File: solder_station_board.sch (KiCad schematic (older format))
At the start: 34 parts, among them J1 Conn_01x04, J2 Conn_FBA, J3 RT_WELLER, J4 VFD dISPLAY, J5 Conn_FBB, P1 ISP, Q1 IRF9540, Q2 2N7002, U4 TLC272, U5 LT1007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

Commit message: Save the last working stand
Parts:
- removed J2: Conn_FBA, Connector_PinSocket_2.54mm:PinSocket_1x01_P2.54mm_Vertical, symbol Connector_Generic:Conn_01x01
- removed J5: Conn_FBB, Connector_PinSocket_2.54mm:PinSocket_1x01_P2.54mm_Vertical, symbol Connector_Generic:Conn_01x01
- added J2: Conn_FB, Connector_PinSocket_2.54mm:PinSocket_1x02_P2.54mm_Vertical, symbol Connector_Generic:Conn_01x02
- added J6: PWR_15V, Connector_Wire:SolderWirePad_1x02_P5.08mm_Drill1.5mm, symbol Connector_Generic:Conn_01x02
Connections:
- wire segments 177 -> 181
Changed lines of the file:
@@
 	9200 5700 8900 5700
 Wire Wire Line
-	9200 6050 8900 6050
-Text Label 9200 6050 2    50   ~ 0
+	9200 5800 8900 5800
+Text Label 9200 5800 2    50   ~ 0
 FBB
-$Comp
-L Connector_Generic:Conn_01x01 J2
-U 1 1 5B5F78C9
-P 8700 5700
-F 0 "J2" H 8620 5475 50  0000 C CNN
-F 1 "Conn_FBA" H 8620 5566 50  0000 C CNN
-F 2 "Connector_PinSocket_2.54mm:PinSocket_1x01_P2.54mm_Vertical" H 8700 5700 50  0001 C CNN
-F 3 "~" H 8700 5700 50  0001 C CNN
-	1    8700 5700
-	-1   0    0    1
-$EndComp
-$Comp
-L Connector_Generic:Conn_01x01 J5
-U 1 1 5B5F79C7
-P 8700 6050
-F 0 "J5" H 8620 5825 50  0000 C CNN
-F 1 "Conn_FBB" H 8620 5916 50  0000 C CNN
-F 2 "Connector_PinSocket_2.54mm:PinSocket_1x01_P2.54mm_Vertical" H 8700 6050 50  0001 C CNN
-F 3 "~" H 8700 6050 50  0001 C CNN
-	1    8700 6050
-	-1   0    0    1
-$EndComp
 $Comp
 L Connector_Generic:Conn_01x04 J1
@@
 Wire Wire Line
 	7600 6150 7450 6150
+$Comp
+L Connector_Generic:Conn_01x02 J6
+U 1 1 5B62CB4A
+P 6100 6550
+F 0 "J6" H 6020 6225 50  0000 C CNN
+F 1 "PWR_15V" H 6020 6316 50  0000 C CNN
+F 2 "Connector_Wire:SolderWirePad_1x02_P5.08mm_Drill1.5mm" H 6100 6550 50  0001 C CNN
+F 3 "~" H 6100 6550 50  0001 C CNN
+	1    6100 6550
+	-1   0    0    1
+$EndComp
+$Comp
+L power:+15V #PWR0128
+U 1 1 5B62CCAC
+P 6500 6250
+F 0 "#PWR0128" H 6500 6100 50  0001 C CNN
+F 1 "+15V" H 6515 6423 50  0000 C CNN
+F 2 "" H 6500 6250 50  0001 C CNN
+F 3 "" H 6500 6250 50  0001 C CNN
+	1    6500 6250
+	1    0    0    -1
+$EndComp
+$Comp
+L power:GND #PWR0129
+U 1 1 5B62CDBA
+P 6500 6700
+F 0 "#PWR0129" H 6500 6450 50  0001 C CNN
+F 1 "GND" H 6505 6527 50  0000 C CNN
+F 2 "" H 6500 6700 50  0001 C CNN
+F 3 "" H 6500 6700 50  0001 C CNN
+	1    6500 6700
+	1    0    0    -1
+$EndComp
+Wire Wire Line
+	6500 6700 6500 6550
+Wire Wire Line
+	6500 6550 6300 6550
+Wire Wire Line
+	6300 6450 6500 6450
+Wire Wire Line
+	6500 6450 6500 6250
+$Comp
+L Connector_Generic:Conn_01x02 J2
+U 1 1 5B63F99D
+P 8700 5800
+F 0 "J2" H 8620 5475 50  0000 C CNN
+F 1 "Conn_FB" H 8620 5566 50  0000 C CNN
+F 2 "Connector_PinSocket_2.54mm:PinSocket_1x02_P2.54mm_Vertical" H 8700 5800 50  0001 C CNN
+F 3 "~" H 8700 5800 50  0001 C CNN
+	1    8700 5800
+	-1   0    0    1
+$EndComp
 $EndSCHEMATC

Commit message: Add inputs and refine
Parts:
- added J5: INPUT, Connector_PinSocket_2.54mm:PinSocket_1x03_P2.54mm_Vertical, symbol Connector_Generic:Conn_01x03
- added J7: INT_PWR, Connector_PinHeader_2.54mm:PinHeader_2x02_P2.54mm_Vertical, symbol Connector_Generic:Conn_02x02_Top_Bottom
- added J8: SERIAL, Connector_PinHeader_2.54mm:PinHeader_1x03_P2.54mm_Vertical, symbol Connector_Generic:Conn_01x03
- added R1, R2, R3: 1k, Resistor_SMD:R_0805_2012Metric_Pad1.15x1.40mm_HandSolder, symbol Device:R_Small
- J1: value Conn_01x04 -> PWR_5_36
- R10, R15, R5: footprint Resistor_SMD:R_0805_2012Metric_Pad1.15x1.40mm_HandSolder -> Resistor_SMD:R_1206_3216Metric_Pad1.42x1.75mm_HandSolder
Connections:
- net labels added: INP1, INP2, INP3
- wire segments 181 -> 211
- no-connect marks 34 -> 29
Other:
- moved on the sheet: J1, J2, J6

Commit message: Add more inputs
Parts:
- added J9: INPUT, Connector_PinSocket_2.54mm:PinSocket_1x03_P2.54mm_Vertical, symbol Connector_Generic:Conn_01x03
- R1, R2, R3: value 1k -> 0; footprint Resistor_SMD:R_0805_2012Metric_Pad1.15x1.40mm_HandSolder -> Resistor_SMD:R_1206_3216Metric_Pad1.42x1.75mm_HandSolder
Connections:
- net labels added: INP4, INP5, INP6
- wire segments 211 -> 208
- no-connect marks 29 -> 26
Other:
- moved on the sheet: J5
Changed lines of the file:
@@
 NoConn ~ 6550 3250
 NoConn ~ 6550 3350
-NoConn ~ 6550 5450
-NoConn ~ 6550 5250
-NoConn ~ 6550 5350
 NoConn ~ 3050 -4000
 $Comp
@@
 L Connector_Generic:Conn_01x03 J5
 U 1 1 5BC945DB
-P 5300 7300
-F 0 "J5" H 5380 7342 50  0000 L CNN
-F 1 "INPUT" H 5380 7251 50  0000 L CNN
-F 2 "Connector_PinSocket_2.54mm:PinSocket_1x03_P2.54mm_Vertical" H 5300 7300 50  0001 C CNN
-F 3 "~" H 5300 7300 50  0001 C CNN
-	1    5300 7300
+P 5250 6750
+F 0 "J5" H 5330 6792 50  0000 L CNN
+F 1 "INPUT" H 5330 6701 50  0000 L CNN
+F 2 "Connector_PinSocket_2.54mm:PinSocket_1x03_P2.54mm_Vertical" H 5250 6750 50  0001 C CNN
+F 3 "~" H 5250 6750 50  0001 C CNN
+	1    5250 6750
 	1    0    0    -1
 $EndComp
@@
 Text Label 6900 5150 2    50   ~ 0
 INP3
-Text Label 4250 7200 0    50   ~ 0
+Text Label 4550 6650 0    50   ~ 0
 INP1
-Text Label 4250 7300 0    50   ~ 0
+Text Label 4550 6750 0    50   ~ 0
 INP2
-Text Label 4250 7400 0    50   ~ 0
+Text Label 4550 6850 0    50   ~ 0
 INP3
-$Comp
-L power:+5V #PWR0131
-U 1 1 5BC9C22F
-P 4800 6400
-F 0 "#PWR0131" H 4800 6250 50  0001 C CNN
-F 1 "+5V" H 4815 6573 50  0000 C CNN
-F 2 "" H 4800 6400 50  0001 C CNN
-F 3 "" H 4800 6400 50  0001 C CNN
-	1    4800 6400
-	1    0    0    -1
-$EndComp
-$Comp
-L Device:R_Small R1
-U 1 1 5BCB8FC7
-P 4650 6750
-F 0 "R1" H 4709 6796 50  0000 L CNN
-F 1 "1k" H 4709 6705 50  0000 L CNN
-F 2 "Resistor_SMD:R_0805_2012Metric_Pad1.15x1.40mm_HandSolder" H 4650 6750 50  0001 C CNN
-F 3 "~" H 4650 6750 50  0001 C CNN
-	1    4650 6750
-	1    0    0    -1
-$EndComp
-$Comp
-L Device:R_Small R2
-U 1 1 5BCC199B
-P 4800 6750
-F 0 "R2" H 4859 6796 50  0000 L CNN
-F 1 "1k" H 4859 6705 50  0000 L CNN
-F 2 "Resistor_SMD:R_0805_2012Metric_Pad1.15x1.40mm_HandSolder" H 4800 6750 50  0001 C CNN
-F 3 "~" H 4800 6750 50  0001 C CNN
-	1    4800 6750
-	1    0    0    -1
-$EndComp
-$Comp
-L Device:R_Small R3
-U 1 1 5BCC3B1E
-P 4950 6750
-F 0 "R3" H 5009 6796 50  0000 L CNN
-F 1 "1k" H 5009 6705 50  0000 L CNN
-F 2 "Resistor_SMD:R_0805_2012Metric_Pad1.15x1.40mm_HandSolder" H 4950 6750 50  0001 C CNN
-F 3 "~" H 4950 6750 50  0001 C CNN
-	1    4950 6750
-	1    0    0    -1
-$EndComp
-Wire Wire Line
-	4800 6400 4800 6500
-Wire Wire Line
-	4800 6850 4800 7300
-Wire Wire Line
-	4250 7300 4800 7300
-Connection ~ 4800 7300
-Wire Wire Line
-	4250 7200 4650 7200
-Wire Wire Line
-	4650 6850 4650 7200
-Connection ~ 4650 7200
-Wire Wire Line
-	4650 6650 4650 6500
-Wire Wire Line
-	4650 6500 4800 6500
-Connection ~ 4800 6500
-Wire Wire Line
-	4800 6500 4800 6650
-Wire Wire Line
-	4800 6500 4950 6500
-Wire Wire Line
-	4950 6500 4950 6650
-Wire Wire Line
-	4650 7200 5100 7200
-Wire Wire Line
-	4800 7300 5100 7300
-Wire Wire Line
-	4250 7400 4950 7400
-Wire Wire Line
-	4950 6850 4950 7400
-Connection ~ 4950 7400
-Wire Wire Line
-	4950 7400 5100 7400
 $Comp
 L Connector_Generic:Conn_02x02_Top_Bottom J7
@@
 	6600 7250 6600 7350
 Connection ~ 6600 7350
+Wire Wire Line
+	4550 6750 5050 6750
+Wire Wire Line
+	4550 6650 5050 6650
+Wire Wire Line
+	4550 6850 5050 6850
+Wire Wire Line
+	6550 5250 6900 5250
+Wire Wire Line
+	6550 5350 6900 5350
+Wire Wire Line
+	6550 5450 6900 5450
+Text Label 6900 5250 2    50   ~ 0
+INP4
+Text Label 6900 5350 2    50   ~ 0
+INP5
+Text Label 6900 5450 2    50   ~ 0
+INP6
+$Comp
+L Connector_Generic:Conn_01x03 J9
+U 1 1 5BF5FFB0
+P 5250 7250
+F 0 "J9" H 5330 7292 50  0000 L CNN
+F 1 "INPUT" H 5330 7201 50  0000 L CNN
+F 2 "Connector_PinSocket_2.54mm:PinSocket_1x03_P2.54mm_Vertical" H 5250 7250 50  0001 C CNN
+F 3 "~" H 5250 7250 50  0001 C CNN
+	1    5250 7250
+	1    0    0    -1
+$EndComp
+Text Label 4450 7150 0    50   ~ 0
+INP4
+Text Label 4450 7250 0    50   ~ 0
+INP5
+Text Label 4450 7350 0    50   ~ 0
+INP6
+Wire Wire Line
+	4450 7150 4700 7150
+$Comp
+L Device:R_Small R1
+U 1 1 5BF6D2C5
+P 4800 7150
+F 0 "R1" V 4750 7200 50  0000 L CNN
+F 1 "0" V 4800 7100 50  0000 L CNN
+F 2 "Resistor_SMD:R_1206_3216Metric_Pad1.42x1.75mm_HandSolder" H 4800 7150 50  0001 C CNN
+F 3 "~" H 4800 7150 50  0001 C CNN
+	1    4800 7150
+	0    1    1    0
+$EndComp
+Wire Wire Line
+	4900 7150 5050 7150
+Wire Wire Line
+	4450 7250 4700 7250
+Wire Wire Line
+	4450 7350 4700 7350
+$Comp
+L Device:R_Small R2
+U 1 1 5BFCBE84
+P 4800 7250
+F 0 "R2" V 4750 7300 50  0000 L CNN
+F 1 "0" V 4800 7200 50  0000 L CNN
+F 2 "Resistor_SMD:R_1206_3216Metric_Pad1.42x1.75mm_HandSolder" H 4800 7250 50  0001 C CNN
+F 3 "~" H 4800 7250 50  0001 C CNN
+	1    4800 7250
+	0    1    1    0
+$EndComp
+Wire Wire Line
+	4900 7250 5050 7250
+$Comp
+L Device:R_Small R3
+U 1 1 5BFCD156
+P 4800 7350
+F 0 "R3" V 4750 7400 50  0000 L CNN
+F 1 "0" V 4800 7300 50  0000 L CNN
+F 2 "Resistor_SMD:R_1206_3216Metric_Pad1.42x1.75mm_HandSolder" H 4800 7350 50  0001 C CNN
+F 3 "~" H 4800 7350 50  0001 C CNN
+	1    4800 7350
+	0    1    1    0
+$EndComp
+Wire Wire Line
+	4900 7350 5050 7350
 $EndSCHEMATC

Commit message: compensate the delta voltage input with resistors
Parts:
- added R? (x2): 1k, Resistor_SMD:R_1206_3216Metric_Pad1.42x1.75mm_HandSolder, symbol Device:R_Small
- J4: footprint Connector_PinSocket_2.54mm:PinSocket_1x34_P2.54mm_Vertical -> Connector_PinSocket_2.54mm:PinSocket_1x34_P2.54mm_Vertical_SMD_Pin1Right
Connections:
- wire segments 208 -> 210
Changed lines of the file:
@@
 EESchema Schematic File Version 4
 LIBS:solder_station_board-cache
-EELAYER 28 0
+EELAYER 29 0
 EELAYER END
 $Descr A4 11693 8268
@@
 	4200 1600 4300 1600
 Wire Wire Line
-	4200 1600 4200 2000
+	4200 1600 4200 1700
 Wire Wire Line
 	4500 1000 4200 1000
@@
 	5500 1700 5600 1700
 Wire Wire Line
-	5500 1700 5500 2100
+	5500 1700 5500 1800
 Wire Wire Line
 	5800 1100 5500 1100
@@
 F 0 "J4" H 10630 3942 50  0000 L CNN
 F 1 "VFD dISPLAY" H 10300 5700 50  0000 L CNN
-F 2 "Connector_PinSocket_2.54mm:PinSocket_1x34_P2.54mm_Vertical" H 10550 3950 50  0001 C CNN
+F 2 "Connector_PinSocket_2.54mm:PinSocket_1x34_P2.54mm_Vertical_SMD_Pin1Right" H 10550 3950 50  0001 C CNN
 F 3 "~" H 10550 3950 50  0001 C CNN
 	1    10550 3950
@@
 Text Label 9950 5350 0    50   ~ 0
 S11
-Text Label 9950 4750 0    50   ~ 0
+Text Label 9950 5450 0    50   ~ 0
 S10
 Wire Wire Line
 	9950 5250 10350 5250
-Text Label 9950 4450 0    50   ~ 0
-1G
-Text Label 9950 4650 0    50   ~ 0
-S12
-Wire Wire Line
-	9950 5150 10350 5150
-Wire Wire Line
-	10350 5050 9950 5050
-Wire Wire Line
-	9950 4950 10350 4950
-Text Label 9950 4350 0    50   ~ 0
-b
-Text Label 9950 4550 0    50   ~ 0
-a
 Text Label 9950 4850 0    50   ~ 0
 1G
+Text Label 9950 5150 0    50   ~ 0
+S12
+Wire Wire Line
+	9950 5150 10350 5150
+Wire Wire Line
+	10350 5050 9950 5050
+Wire Wire Line
+	9950 4950 10350 4950
+Text Label 9950 4950 0    50   ~ 0
+b
+Text Label 9950 5050 0    50   ~ 0
+a
+Text Label 9950 5250 0    50   ~ 0
+1G
 Wire Wire Line
 	9950 4850 10350 4850
@@
 Wire Wire Line
 	9950 4750 10350 4750
-Text Label 9950 4950 0    50   ~ 0
+Text Label 9950 4750 0    50   ~ 0
 c
-Text Label 9950 5050 0    50   ~ 0
+Text Label 9950 4650 0    50   ~ 0
 d
-Text Label 9950 5150 0    50   ~ 0
+Text Label 9950 4550 0    50   ~ 0
 2G
 Text Label 9950 2550 0    50   ~ 0
@@
 Text Label 9950 4250 0    50   ~ 0
 3G
-Text Label 9950 5450 0    50   ~ 0
+Text Label 9950 4350 0    50   ~ 0
 f
-Text Label 9950 5250 0    50   ~ 0
+Text Label 9950 4450 0    50   ~ 0
 e
 Wire Wire Line
 	9250 3050 9500 3050
-Text Label 9500 4550 2    50   ~ 0
+Text Label 9500 4150 2    50   ~ 0
 1G
-Text Label 9500 4250 2    50   ~ 0
+Text Label 9500 4850 2    50   ~ 0
 2G
 Text Label 9500 3050 2    50   ~ 0
@@
 Wire Wire Line
 	9500 4950 9250 4950
+Text Label 9500 4350 2    50   ~ 0
+a
+Text Label 9500 4450 2    50   ~ 0
+b
+Text Label 9500 4550 2    50   ~ 0
+c
+Text Label 9500 4950 2    50   ~ 0
+d
 Text Label 9500 4750 2    50   ~ 0
-a
+e
 Text Label 9500 4650 2    50   ~ 0
-b
-Text Label 9500 4450 2    50   ~ 0
-c
-Text Label 9500 4350 2    50   ~ 0
-d
-Text Label 9500 4150 2    50   ~ 0
-e
-Text Label 9500 4050 2    50   ~ 0
 f
 Text Label 9500 3150 2    50   ~ 0
 g
-Text Label 9500 4850 2    50   ~ 0
+Text Label 9500 4250 2    50   ~ 0
 S12
-Text Label 9500 4950 2    50   ~ 0
+Text Label 9500 4050 2    50   ~ 0
 S10
 Text Notes 7350 2250 0    89   ~ 0
@@
 Wire Wire Line
 	4900 7350 5050 7350
+Wire Wire Line
+	4200 1900 4200 2000
+$Comp
+L Device:R_Small R?
+U 1 1 5C108751
+P 5500 1900
+F 0 "R?" V 5696 1900 50  0000 C CNN
+F 1 "1k" V 5605 1900 50  0000 C CNN
+F 2 "Resistor_SMD:R_1206_3216Metric_Pad1.42x1.75mm_HandSolder" H 5500 1900 50  0001 C CNN
+F 3 "~" H 5500 1900 50  0001 C CNN
+	1    5500 1900
+	1    0    0    -1
+$EndComp
+Wire Wire Line
+	5500 2000 5500 2100
+$Comp
+L Device:R_Small R?
+U 1 1 5C108287
+P 4200 1800
+F 0 "R?" V 4396 1800 50  0000 C CNN
+F 1 "1k" V 4305 1800 50  0000 C CNN
+F 2 "Resistor_SMD:R_1206_3216Metric_Pad1.42x1.75mm_HandSolder" H 4200 1800 50  0001 C CNN
+F 3 "~" H 4200 1800 50  0001 C CNN
+	1    4200 1800
+	1    0    0    -1
+$EndComp
 $EndSCHEMATC

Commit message: add resistor to the + input of opamp
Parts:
- removed D3, D7: 1N4148, Diode_SMD:D_MiniMELF_Handsoldering, symbol Device:D
- removed R1, R2, R3: 0, Resistor_SMD:R_1206_3216Metric_Pad1.42x1.75mm_HandSolder, symbol Device:R_Small
- added C1, C2: 10n, Capacitor_SMD:C_0805_2012Metric_Pad1.15x1.40mm_HandSolder, symbol Device:C_Small
- added D1: BAT54S, Package_TO_SOT_SMD:SOT-23, symbol Diode:BAT54S
- added TP1, TP2, TP3: tp, Connector_Wire:SolderWirePad_1x01_Drill0.8mm, symbol Connector:TestPoint
- D8: footprint Diode_SMD:D_MiniMELF_Handsoldering -> Diode_SMD:D_MicroMELF_Hadsoldering
- P1: symbol custom:ISP -> solder_station_board-rescue:ISP-custom
- R10, R11, R15, R5, R9: footprint Resistor_SMD:R_1206_3216Metric_Pad1.42x1.75mm_HandSolder -> Resistor_SMD:R_0805_2012Metric_Pad1.15x1.40mm_HandSolder
- R16, R4: renamed from R?; footprint Resistor_SMD:R_1206_3216Metric_Pad1.42x1.75mm_HandSolder -> Resistor_SMD:R_0805_2012Metric_Pad1.15x1.40mm_HandSolder
- U6: symbol atmel:ATMEGA168-20AU -> solder_station_board-rescue:ATMEGA168-20AU-atmel
- U7: symbol custom:HV5812-SOIC -> solder_station_board-rescue:HV5812-SOIC-custom
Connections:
- wire segments 210 -> 216
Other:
- moved on the sheet: C13, R4

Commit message: ready to version
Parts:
- TP1, TP2, TP3: symbol Connector:TestPoint -> solder_station_board-rescue:TestPoint-Connector
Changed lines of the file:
@@
 EESchema Schematic File Version 4
 LIBS:solder_station_board-cache
-EELAYER 26 0
+EELAYER 29 0
 EELAYER END
 $Descr A4 11693 8268
@@
 Connection ~ 6350 1100
 $Comp
-L Connector:TestPoint TP1
+L solder_station_board-rescue:TestPoint-Connector TP1
 U 1 1 5BFA584B
 P 3750 950
@@
 $EndComp
 $Comp
-L Connector:TestPoint TP2
+L solder_station_board-rescue:TestPoint-Connector TP2
 U 1 1 5BFA5B5B
 P 5250 1000
@@
 $EndComp
 $Comp
-L Connector:TestPoint TP3
+L solder_station_board-rescue:TestPoint-Connector TP3
 U 1 1 5BFA5C52
 P 6850 1000

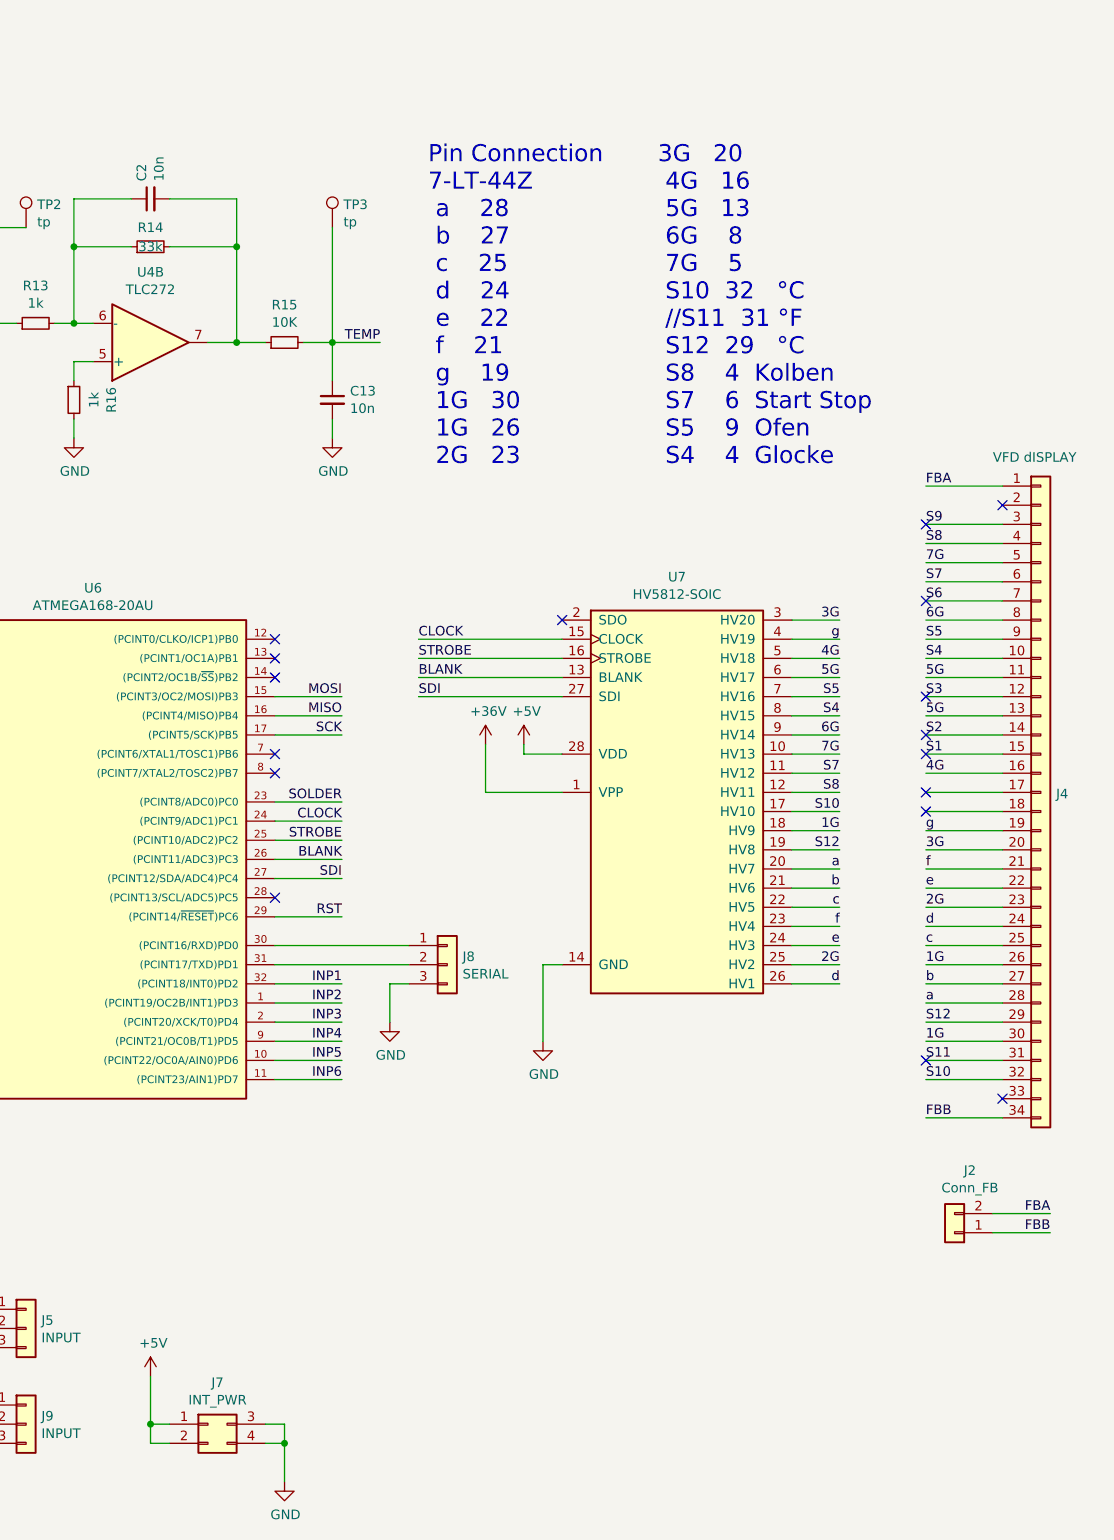
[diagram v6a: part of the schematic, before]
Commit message: remove the vfd display and driver from the schematic.
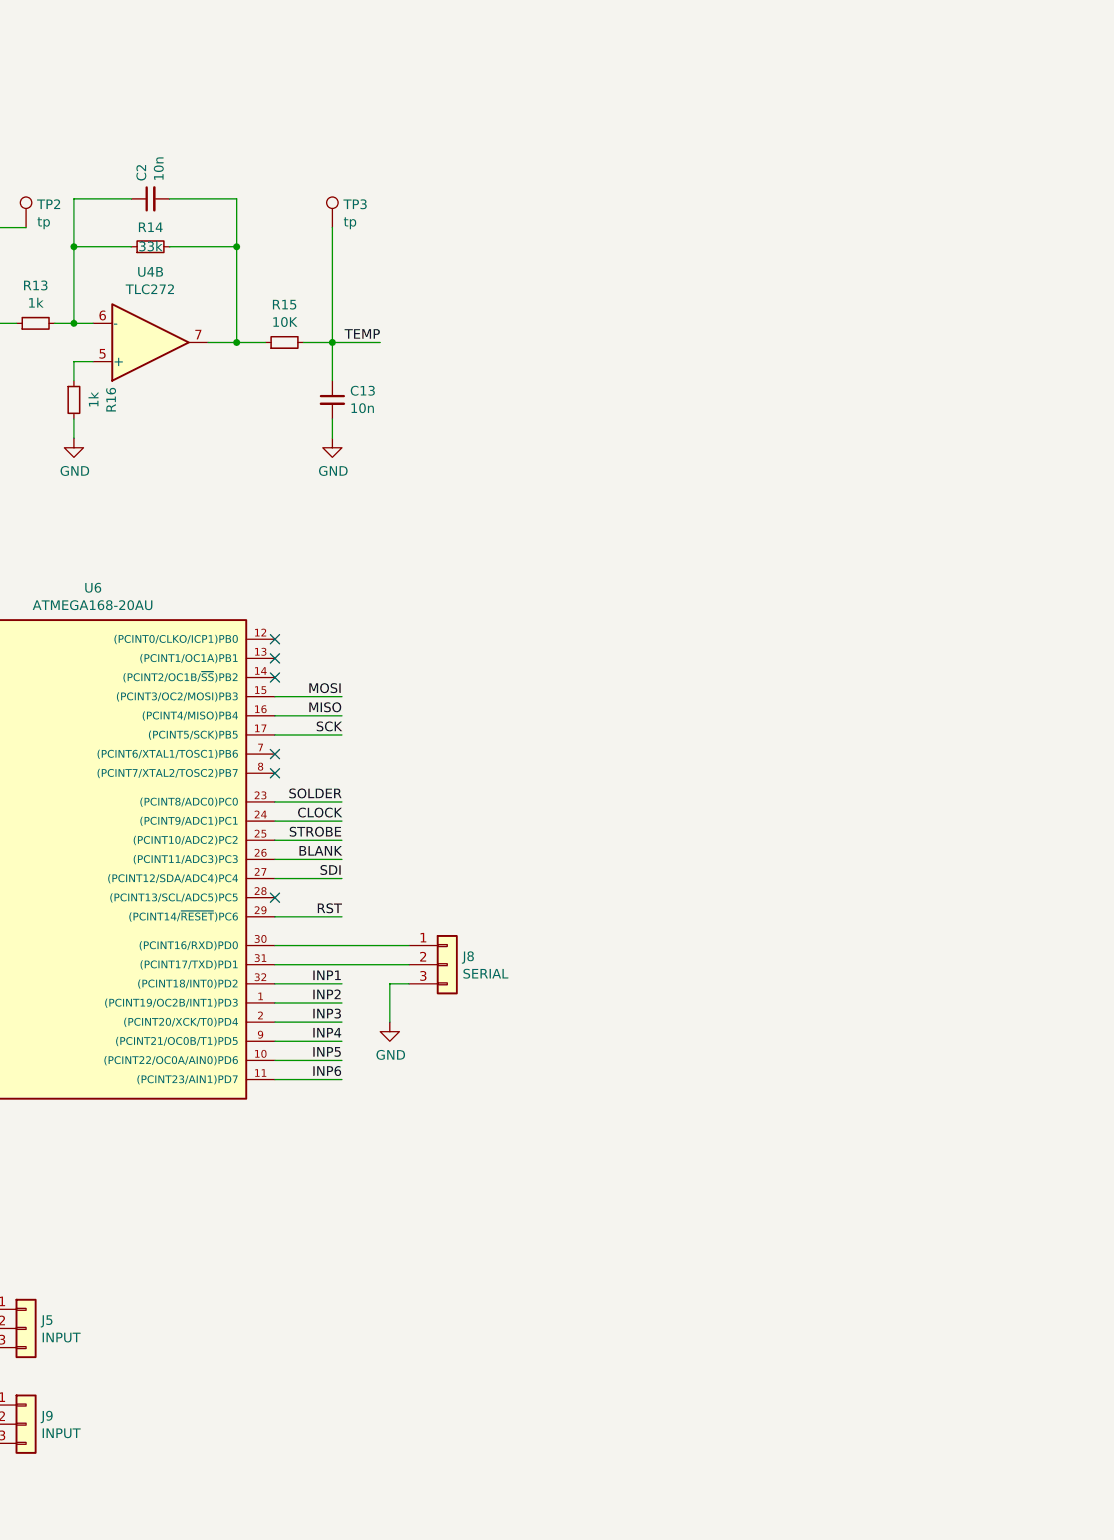
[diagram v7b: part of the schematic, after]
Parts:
- removed J2: Conn_FB, Connector_PinSocket_2.54mm:PinSocket_1x02_P2.54mm_Vertical, symbol Connector_Generic:Conn_01x02
- removed J4: VFD dISPLAY, Connector_PinSocket_2.54mm:PinSocket_1x34_P2.54mm_Vertical_SMD_Pin1Right, symbol Connector_Generic:Conn_01x34
- removed J7: INT_PWR, Connector_PinHeader_2.54mm:PinHeader_2x02_P2.54mm_Vertical, symbol Connector_Generic:Conn_02x02_Top_Bottom
- removed U7: HV5812-SOIC, Package_SO:SOIC-28W_7.5x18.7mm_P1.27mm, symbol solder_station_board-rescue:HV5812-SOIC-custom
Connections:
- no-connect marks 26 -> 15
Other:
- note removed: "3G 20\n 4G 16\n 5G 13\n 6G 8\n 7G 5\n S10 32 °C\n //S11 31 °F\n S12 29 °C\n S8 4 Kolben\n S7 6 Start Stop\n S5 9 Ofen\n S4 4 Glocke"
- note removed: "Pin Connection \n7-LT-44Z\n a 28\n b 27\n c 25\n d 24\n e 22\n f 21\n g 19\n 1G 30\n 1G 26\n 2G 23"
